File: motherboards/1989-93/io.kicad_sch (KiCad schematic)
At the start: 16 parts, among them J2 LSU 4.9, J3 IAT, J4 USB-C, J5 AUX 2x8, U2 MPX5700AP, U4 USBLC6-2SC6

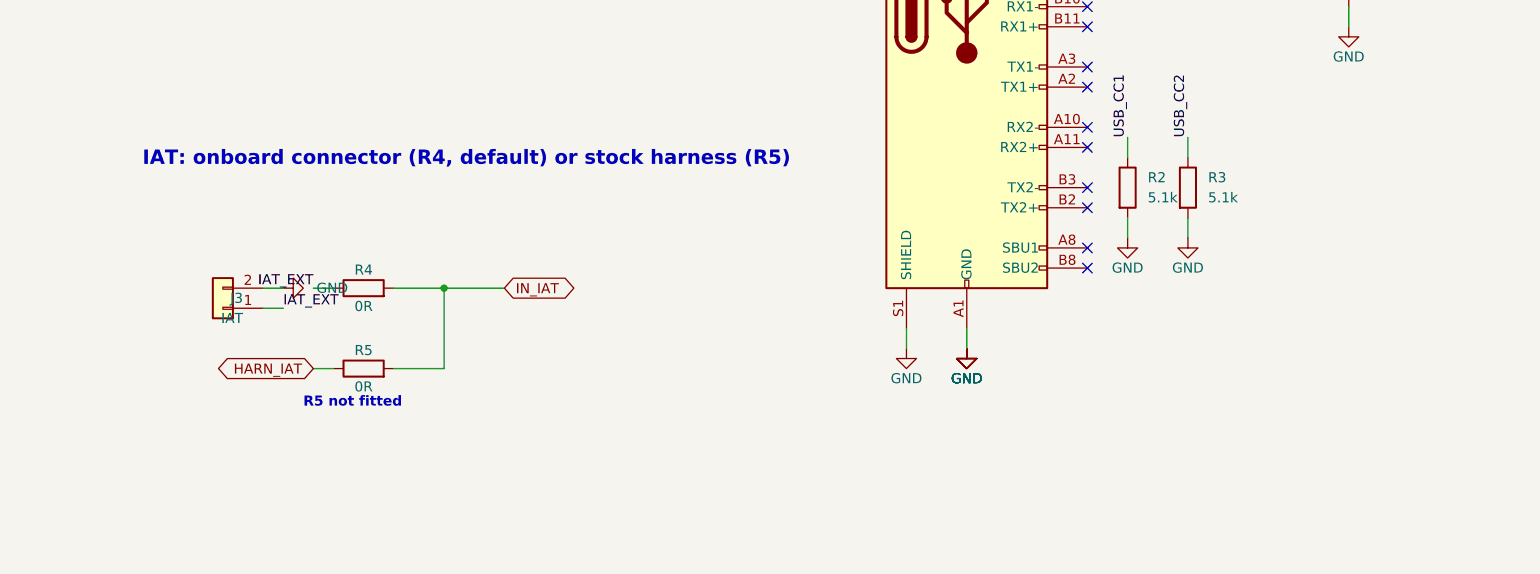
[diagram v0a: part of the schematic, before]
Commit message: IAT source jumper on every motherboard; wideband MCU flashed through the main MCU
- motherboards (1989-93 / 1994-95 rev 0.5, 1996-97 / 1999-2000 / 2001-05
  rev 0.3): the R4/R5 0R links are replaced by JP1, a 1x3 2.54 mm header with
  a removable shunt (STOCK = harness sensor, EXT = IAT connector, default)
- daughterboard rev 0.4: USART3 (PD8/PD9) to the STM32F042's ROM-bootloader
  USART1 (PA9/PA10), plus PD10 -> its BOOT0 and PD11 -> its NRST, so both
  MCUs can be flashed over the one USB-C port (rusEFI support to be written;
  SWD pads kept as a fallback)
- scripts: schematic check now also catches nets split across sheets;
  motherboard project template bundled
- README: flashing and IAT sections

Co-Authored-By: Claude Opus 5.5 <noreply@anthropic.com>
Claude-Session: https://claude.ai/code/session_012UFcA8PhPqkqYxcgEjD2n9
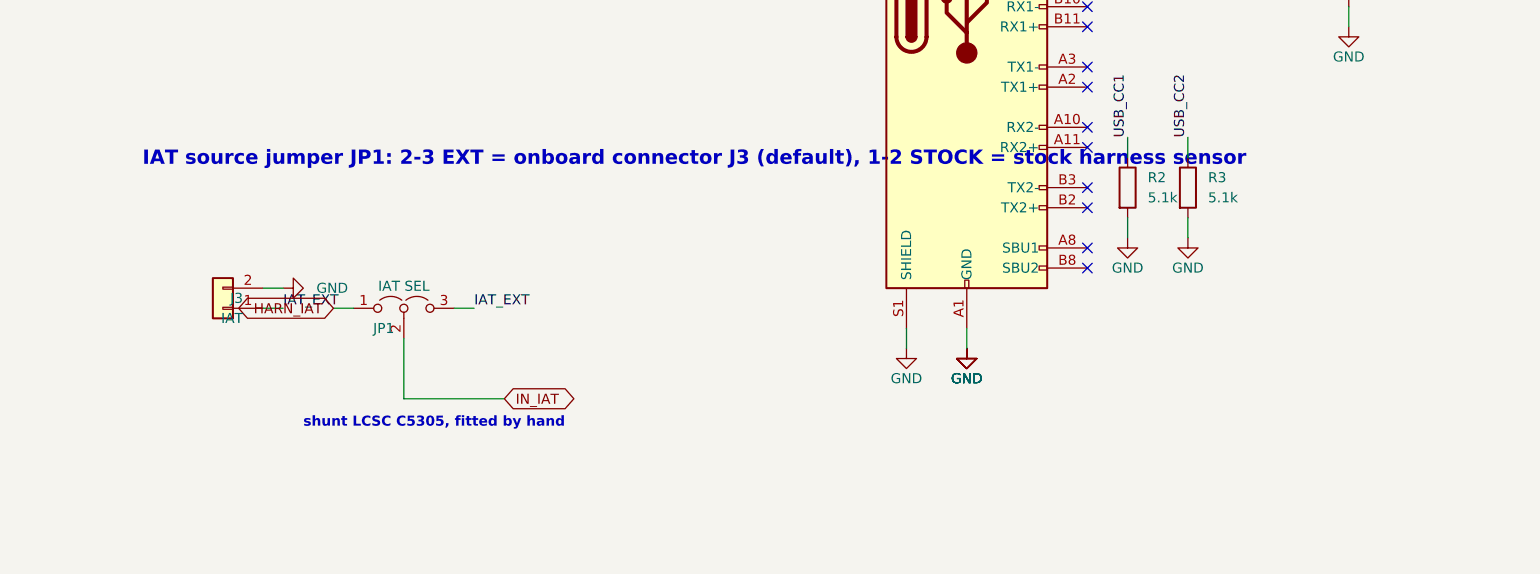
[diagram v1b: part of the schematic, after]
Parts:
- removed R4, R5: 0R, Resistor_SMD:R_0603_1608Metric, symbol Device:R
- added JP1: IAT SEL, Connector_PinHeader_2.54mm:PinHeader_1x03_P2.54mm_Vertical, symbol Jumper:Jumper_3_Open
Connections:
- net HARN_IAT: now also JP1.1 (A)
- net IAT_EXT: now also JP1.3 (B)
- net IN_IAT: now also JP1.2 (C)
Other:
- note added: "IAT source jumper JP1: 2-3 EXT = onboard connector J3 (default), 1-2 STOCK = stock harness sensor"
- note added: "shunt LCSC C5305, fitted by hand"
- note removed: "IAT: onboard connector (R4, default) or stock harness (R5)"
- note removed: "R5 not fitted"

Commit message: Rev 0.5 daughterboard, rev 0.6 1989-93/1994-95 motherboards: review fixes
Daughterboard rev 0.5:
- SN74LVC4245A drives the eight AUIPS2041 low sides at 5 V; output enable pulled
  off (R71) until the firmware enables it on PA8.
- BOOT1 pull-down (R72); hall input clamps D13/D14.
- ULN2003 COM to an SMAJ33A TVS (D11) instead of +12V: no key-off back-feed,
  no conduction in a 35 V load dump.
- Logic supply: D7/D8 -> 0.5 A PTC F1 -> SMAJ33A D12; C16 50 V, SS36 D9, C59.
- Tach stays an output.

Motherboards:
- Idle/VVT freewheel diodes, 4.7k switch pull-up options (not fitted),
  AUX VBAT PTC on all years.
- 1989-93 rev 0.6: two drivers per injector wire (0R links), SMCJ40A clamps.
- 2001-05: J1 3B tied to 3A.

Firmware: low-side enable (inverted open drain, forced writes, off during
configuration changes), unused control pins parked with pull-down, 1989-93
batch on all four outputs, VBATT offset noted.

Verification: 18/18 board tests, 119/119 harness check, circuit sims
20 OK / 3 CHECK / 6 REF / 0 FAIL, flash sim 9/9, firmware and bootloader
build; all boards 0 unconnected, 0 clearance errors.

Co-Authored-By: Claude Opus 5.5 <noreply@anthropic.com>
Claude-Session: https://claude.ai/code/session_012UFcA8PhPqkqYxcgEjD2n9
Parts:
- added D1, D2: SS34, Diode_SMD:D_SMA, symbol Device:D_Schottky
- added D3, D4: SMCJ40A, Diode_SMD:D_SMC, symbol Device:D_Zener
- added F4: 0.5A hold, Fuse:Fuse_1206_3216Metric, symbol Device:Polyfuse
- added R20, R21, R22: 4.7k, Resistor_SMD:R_0603_1608Metric, symbol Device:R
- added R23, R24, R25, R26: 0R, Resistor_SMD:R_0805_2012Metric, symbol Device:R
- J5: Note Add-on I/O: COP 3/4, boost, alternator, main relay, knock, VR crank/cam, external AFR, UART, 5 V, +12 V -> Add-on I/O: COP 3/4, boost, alternator, main relay, knock, VR crank/cam, external AFR, UART, 5 V, +12 V (fused, F4)
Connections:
- net GND: now also D3.2 (A), D4.2 (A)
- net VBAT_IN: now also D1.1 (K), D2.1 (K), F4.1, R20.1, R21.1, R22.1; no longer J5.15 (Pin_15)
- new net AUX_VBAT: F4.2, J5.15 (Pin_15)
- new net HARN_2Y: R25.2
- new net HARN_2Z: R26.2
- new net IN_SW1: R20.2
- new net IN_SW2: R21.2
- new net IN_SW3: R22.2
- new net OUT_IACV: D1.2 (A)
- new net OUT_INJ1: D3.1 (K), R23.2
- new net OUT_INJ2: D4.1 (K), R24.2
- new net OUT_INJ3: R24.1, R25.1
- new net OUT_INJ4: R23.1, R26.1
- new net OUT_VVT: D2.2 (A)
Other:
- note added: "1989-93 batch harness: two drivers per injector wire, TVS clamp per wire"
- note added: "AUX: add-on I/O the stock harness has no pins for (+12 V through F4)"
- note added: "Fused +12 V feeds (harness actuators, AUX)"
- note added: "Sequential conversion: remove R23/R24, fit R25/R26 (never R26 on an automatic)"
- note added: "Switch-input 12 V pull-ups, NOT fitted: fit only for a signal that switches to ground"
- note added: "Valve freewheel diodes (to each valve's +12 V feed) and fit options"
- note removed: "AUX: add-on I/O the stock harness has no pins for"

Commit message: Daughterboard rev 0.5b: LM2903 VR conditioner, JLC placement fix, parts-availability swaps
- U9: the out-of-stock, single-source MAX9926 is replaced by an LM2903 dual comparator (TI, onsemi, UMW, ST...).
  Each VR input gets a BAT54S clamp to GND/+5V and 100k to a 1.65 V bias, each output 1M of hysteresis
  (D15-D18, R73-R80, C60). Same output polarity, so J2 wiring and firmware are unchanged. circuit_sim.py
  section H covers it (25 OK / 4 CHECK / 6 REF / 0 FAIL).
- Re-routed; daughter_patch_05b.py (with hand_route.py) routes HALL1, which the autorouter left open, and
  moves AN_AUX3 clear of the new clamps. Netlist 778 pads, 0 differences; DRC 0 unconnected, 0 clearance.
- CPLs for all boards now use the gerbers' own coordinates, with JLC's per-package rotation offsets
  (SOT-223/TO-252/SOT-23 +180, SOIC/TSSOP/LQFP +270, resistor arrays +90).
- Parts-availability review swaps: motherboard F4 to TECHFUSE nSMD050-33V (C70077; the old PTC is out of
  stock), D6 to Littelfuse SMCJ30A, D9 to Diodes B360A. MPX5700AP (NRND), the harness headers and the
  STM32F042 are recorded as supply open items in VERIFICATION.md.
- Viewer assets and README renders rebuilt.

Co-Authored-By: Claude Opus 5.5 <noreply@anthropic.com>
Claude-Session: https://claude.ai/code/session_012UFcA8PhPqkqYxcgEjD2n9
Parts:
- F4: LCSC C209741 -> C70077; Note Resettable fuse for the AUX +12 V pin J5-15 (SMD1206P050TF/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 -> Resettable fuse for the AUX +12 V pin J5-15 (TECHFUSE nSMD0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
